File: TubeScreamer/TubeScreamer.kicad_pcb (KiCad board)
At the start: 2 copper layers, 44 parts, among them J3 AudioJack2, Q1 2SC1815, Q2 2SC1815, U1 Opamp_Dual_Generic

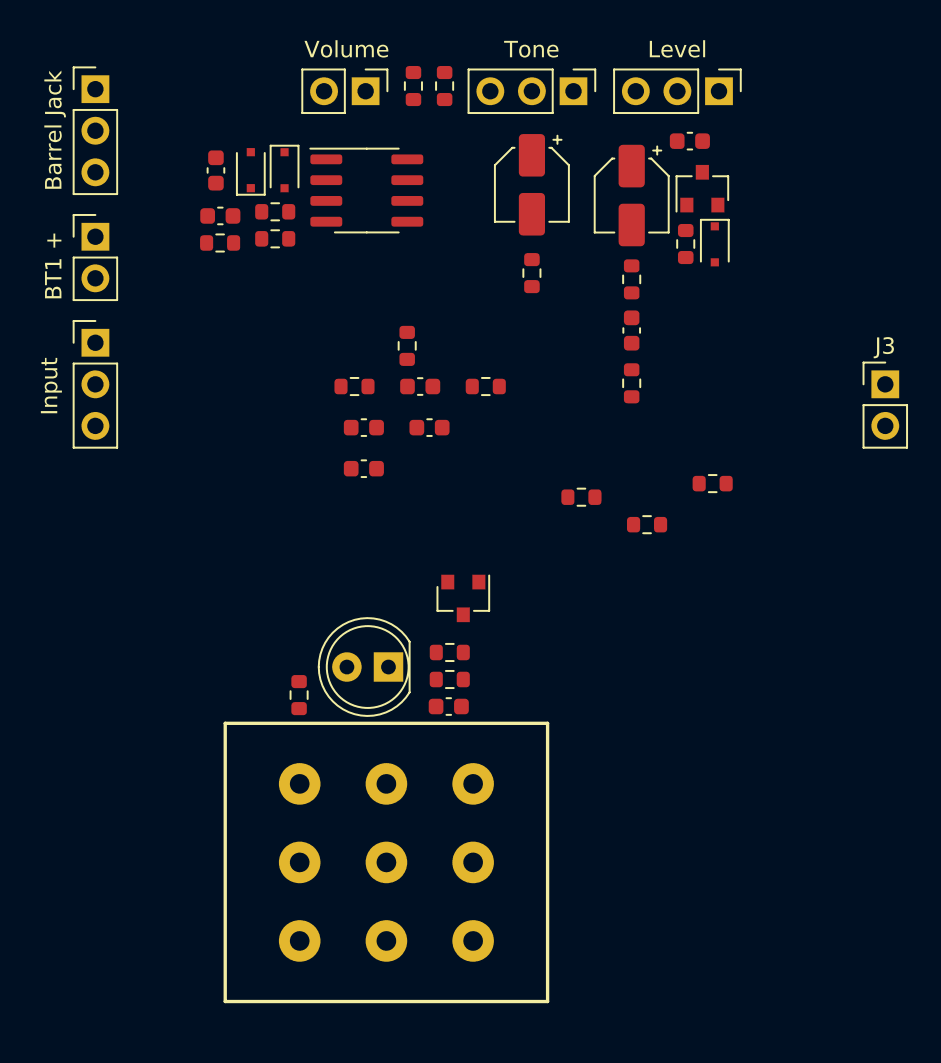
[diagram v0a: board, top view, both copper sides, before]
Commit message: Finalized component locations on pcb. Need to export BOM and pos files
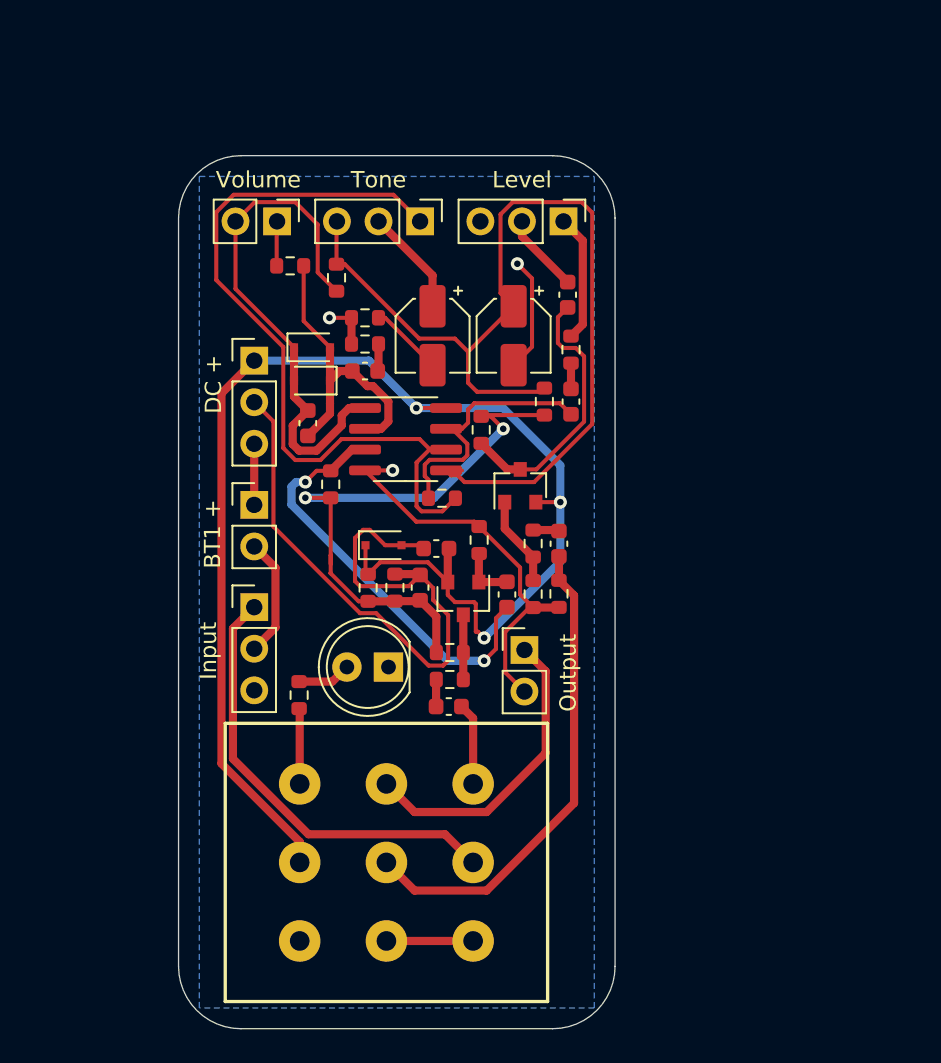
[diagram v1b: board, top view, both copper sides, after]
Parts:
- DC +: renamed from Barrel Jack
- moved Output 27.4 mm to (149.4, 96.2)
- moved D1 27.3 mm to (140.8, 89.8), turned to 0 degrees
- moved R15 23.3 mm to (149.9, 92.8)
- moved R4 22.1 mm to (139.9, 92.4), turned to 90 degrees
- moved Q2 21.3 mm to (149.1, 86.2)
- moved R17 19.7 mm to (151.5, 92.8), turned to 270 degrees
- moved DC + 19.2 mm to (132.9, 78.6)
- moved BT1 + 19.0 mm to (132.9, 87.4)
- moved Input 18.8 mm to (132.9, 93.6)
- moved R7 17.0 mm to (137.6, 86.1), turned to 270 degrees
- moved C6 16.4 mm to (136.2, 82.4)
- moved U1 15.4 mm to (142.1, 83.4)
- moved C11 13.8 mm to (151.5, 89.8), turned to 90 degrees
- moved R9 13.4 mm to (137.9, 73.5), turned to 270 degrees
- moved C4 13.4 mm to (148.3, 92.8), turned to 270 degrees
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- renumbered J3 to Output
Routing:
- net +9V: track 0.00 -> 85.3 mm, vias 0 -> 3
- net Net-(C7-Pad1): track 0.00 -> 60.4 mm
- net Net-(P2-Pad1): track 0.00 -> 48.9 mm
- net Net-(C2-Pad1): track 0.00 -> 41.8 mm
- net 4V5: track 0.00 -> 36.0 mm, vias 0 -> 2
- net GND: track 0.00 -> 34.4 mm, vias 0 -> 3
- net Net-(C6-Pad2): track 0.00 -> 32.5 mm
- net Net-(C11-Pad1): track 0.00 -> 29.8 mm
- net Net-(J2-Pad1): track 0.00 -> 27.1 mm
- net Net-(C4-Pad2): track 0.00 -> 26.5 mm, vias 0 -> 2
- net Net-(C5-Pad2): track 0.00 -> 19.0 mm
- net Net-(J3-Pad1): track 0.00 -> 18.8 mm
- net Net-(C9-Pad2): track 0.00 -> 16.9 mm
- net Net-(C10-Pad1): track 0.00 -> 16.5 mm
- net Net-(P3-Pad1): track 0.00 -> 7.80 mm
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- added copper zone on B.Cu, net GND
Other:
- board outline added: 26.7 x 53.3 mm

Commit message: Added name and version number to silkscreen layer
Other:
- board text added: "Thomas McDonagh mcdonaghcorp.com"
- board text added: "Tube Screamer V1.0"
